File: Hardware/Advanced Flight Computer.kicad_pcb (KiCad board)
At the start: 4 copper layers, 65 x 110 mm, 151 parts, among them CN1 ATGM336H-6N-74, J1 Conn_01x03_Pin, J2 Conn_01x04_Pin, J3 Conn_01x02_Pin, J4 Conn_01x02_Pin, J5 Conn_01x02_Pin, J6 Conn_01x02_Pin, J7 Conn_01x05_Pin, J8 Conn_01x04_Pin, M1 Motor_Servo, M2 Motor_Servo, M3 Motor_Servo, M4 Motor_Servo, M5 Motor_Servo, M6 Motor_Servo, P1 WJ500V-5.08-2P-14-00A, P2 WJ500V-5.08-2P-14-00A, P3 WJ500V-5.08-2P-14-00A, P4 WJ500V-5.08-2P-14-00A, P5 WJ500V-5.08-2P-14-00A, P6 WJ500V-5.08-2P-14-00A, P7 WJ500V-5.08-2P-14-00A, P8 WJ500V-5.08-2P-14-00A, Q1 SI7232DN-T1-GE3, Q2 SI7232DN-T1-GE3, Q3 SI7232DN-T1-GE3, Q7 2N2222AU, SW1 TS-1088-AR02016, SW2 TS-1088-AR02016, U1 BMP580, U10 0438006.WRGT, U11 0438006.WRGT, U12 0438006.WRGT, U13 0438006.WRGT, U2 STM32H743VITx, U3 ICM-45686, U4 LMR51430XDDCR, U5 AP64501SP-13, U6 RA-02, U7 TPS2121RUXR, U8 0438006.WRGT, U9 0438006.WRGT, X1 X322525MOB4SI, X2 Q13FC1350000400

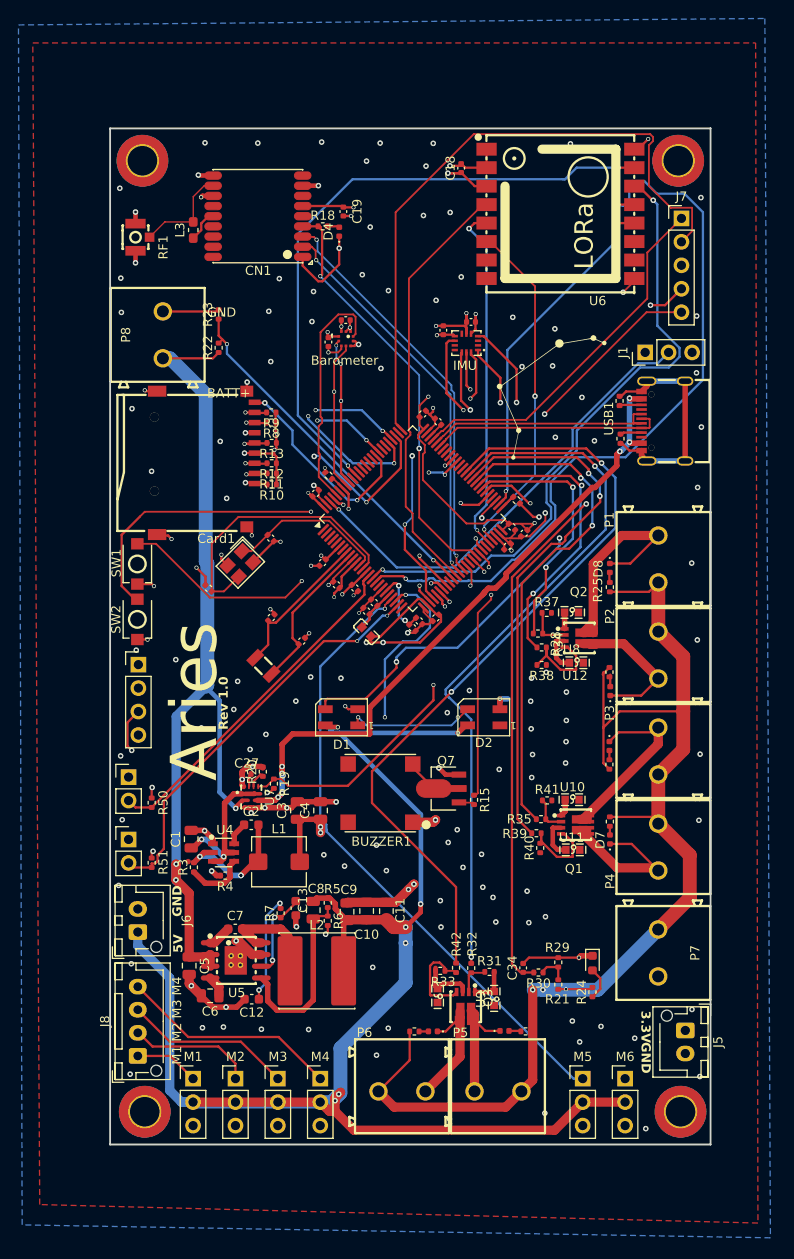
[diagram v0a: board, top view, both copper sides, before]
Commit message: PCB fixes and new production file
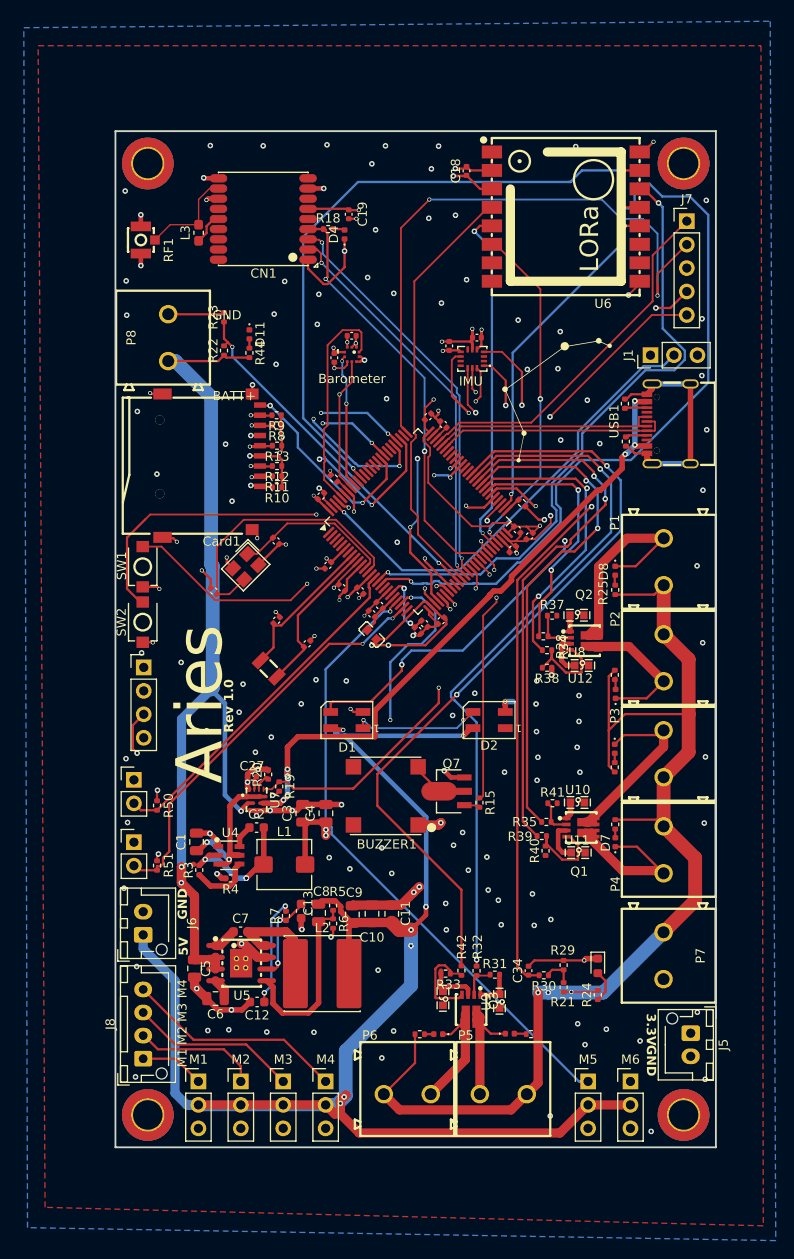
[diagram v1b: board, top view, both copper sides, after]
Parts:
- added D11: LED, LED_SMD:LED_0402_1005Metric, F.Cu at (79.5, 62.0)
- added R44: 430, Resistor_SMD:R_0402_1005Metric, F.Cu at (79.5, 64.0)
- R24: value 530 -> 550
- moved C14 1.82 mm to (88.7, 64.5)
- moved U1 1.82 mm to (90.6, 64.2)
- moved U3 1.82 mm to (103.6, 64.6)
- moved C17 1.82 mm to (101.1, 63.2)
- moved C15 1.82 mm to (90.6, 62.1)
- moved C16 1.82 mm to (104.1, 62.4)
- moved C39 0.65 mm to (75.7, 89.8)
- moved R13 0.65 mm to (82.5, 74.0)
- moved R16 0.65 mm to (110.0, 137.8)
- moved R21 0.65 mm to (113.5, 132.7)
- moved R29 0.65 mm to (113.5, 130.3)
- moved C9 0.65 mm to (90.7, 124.8)
- moved D4 0.65 mm to (89.8, 51.2)
- moved R14 0.65 mm to (88.7, 77.6)
- moved R15 0.65 mm to (104.4, 112.7)
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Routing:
- net +BATT: track 186.6 -> 189.4 mm
- net /SWCLK: track 70.6 -> 67.8 mm, vias 0 -> 2
- net /ICM_CS: track 30.2 -> 28.7 mm
- net /I2C_SCL: track 93.6 -> 92.2 mm, vias 4 -> 3
- net /BMP_INT: track 25.6 -> 24.2 mm
- net /ICM_SCK: track 31.1 -> 29.7 mm
- net /ICM_INT2: track 31.4 -> 30.0 mm
- net /I2C_SDA: track 81.9 -> 80.5 mm
- net /ICM_SDI: track 34.9 -> 33.6 mm
- net Net-(D11-A): track 0.00 -> 1.01 mm
- net /ICM_SDO: track 35.9 -> 35.0 mm
- net GND: track 176.1 -> 176.9 mm, vias 158 -> 159
- net /ICM_INT1: track 43.9 -> 43.2 mm
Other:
- board text added: "Designed by Kian Cheng"
